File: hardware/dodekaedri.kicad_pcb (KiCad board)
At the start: 4 copper layers, 76.2 x 76.2 mm, 227 parts, among them CON401 BARREL_JACK, J801 HANDSFREE, P301 BNC, P801 TX_SW_WIRE, P802 USB_OTG, P803 UART, P804 PROG, P805 RNG_PINS, P806 CONN_01X08, P807 CONN_01X04, P808 CONN_02X04, P809 BOOT0JMPR, Q501 BCP56, Q502 IRL510, Q801 BSS84, SW801 SW_PUSH, SW802 SW, SW803 SW, SW804 SW, SW806 encoder, SW807 RESET, T301 TRANSFO, T302 TRANSFO, T501 TRANSFO2, T601 TRANSFO2, U201 MIC5365, U202 SI5351A, U401 NCP3170-D, U501 74LVC1G3157, U502 74LVC1G3157, U601 74LVC1G3157, U602 74LVC1G3157, U603 TL972IDR, U701 WM8731, U702 MCP6L02, U801 STM32F401, U802 WM8731

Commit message: intermediate save; closing in on the finished layout
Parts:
- C804, D818, R801, R802, R805, R825, R826, R827, R828, R830, R831, R832, R833, R834, R835, W401: moved to B.Cu
- moved R826 247.2 mm to (106.7, 81.7), turned to 270 degrees
- moved R825 244.0 mm to (106.7, 77.0), turned to 270 degrees
- moved R828 243.8 mm to (106.7, 91.1), turned to 270 degrees
- moved R801 238.2 mm to (121.6, 107.4), turned to 45 degrees
- moved R802 234.9 mm to (124.5, 113.2), turned to 315 degrees
- moved R834 231.9 mm to (114.3, 86.4), turned to 270 degrees
- moved R805 221.1 mm to (122.2, 56.8), turned to 315 degrees
- moved R835 221.1 mm to (114.3, 91.1), turned to 270 degrees
- moved R831 218.3 mm to (114.3, 72.2), turned to 270 degrees
- moved R830 213.2 mm to (113.1, 68.5)
- moved R827 207.0 mm to (106.7, 86.4), turned to 270 degrees
- moved R833 205.7 mm to (114.3, 81.7), turned to 270 degrees
- moved D818 197.4 mm to (117.5, 109.0), turned to 45 degrees
- moved R807 194.4 mm to (118.9, 60.0)
- moved R824 192.6 mm to (114.0, 104.2), turned to 45 degrees
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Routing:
- net Net-(P806-Pad6): track 2.63 -> 71.3 mm
- net Net-(P806-Pad7): track 2.92 -> 65.7 mm
- net /CPU/PB3/SWO: track 4.71 -> 59.5 mm, vias 1 -> 2
- net /CPU/PB2: track 1.29 -> 53.3 mm, vias 1 -> 2
- net /CPU/PB10: track 2.47 -> 44.8 mm, vias 1 -> 2
- net +Vlogic: track 116.1 -> 155.7 mm
- net Net-(C804-Pad1): track 1.04 -> 40.4 mm, vias 1 -> 2
- net Net-(P807-Pad1): track 2.50 -> 40.6 mm
- net Net-(P807-Pad3): track 2.71 -> 40.3 mm
- net Net-(P806-Pad3): track 1.96 -> 39.4 mm
- net Net-(P806-Pad8): track 2.44 -> 34.6 mm
- net Net-(P806-Pad5): track 1.59 -> 26.8 mm
- net Net-(P809-Pad1): track 11.8 -> 33.0 mm
- net GND: track 261.6 -> 281.5 mm, vias 23 -> 26
- net /CPU/VIN_ADC: track 0.00 -> 12.5 mm
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
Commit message: Again, managed to advance layout a bit
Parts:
- C802, Q801, R803, R804: moved to B.Cu
- moved R803 83.9 mm to (132.1, 96.0)
- moved R804 61.5 mm to (139.4, 73.2)
- moved C802 57.6 mm to (135.3, 68.6), turned to 180 degrees
- moved Q801 46.0 mm to (138.4, 70.4), turned to 270 degrees
- moved C805 0.59 mm to (136.8, 77.7)
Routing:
- net /CPU/PC14: track 0.00 -> 73.1 mm, vias 0 -> 2
- net /CPU/PD2: track 4.88 -> 73.1 mm, vias 1 -> 2
- net /CPU/PA3: track 1.11 -> 59.0 mm
- net /CPU/RX_TX: track 11.7 -> 25.2 mm, vias 0 -> 1
- net /CPU/CLK_CPU: track 0.00 -> 12.2 mm, vias 0 -> 1
- net Net-(P806-Pad5): track 26.8 -> 35.2 mm
- net +Vlogic: track 155.7 -> 162.3 mm
- net GND: track 281.5 -> 285.1 mm, vias 26 -> 28
- net Net-(Q801-Pad2): track 0.00 -> 2.18 mm
- net /CPU/UI_SW_GRID1: track 12.8 -> 12.3 mm

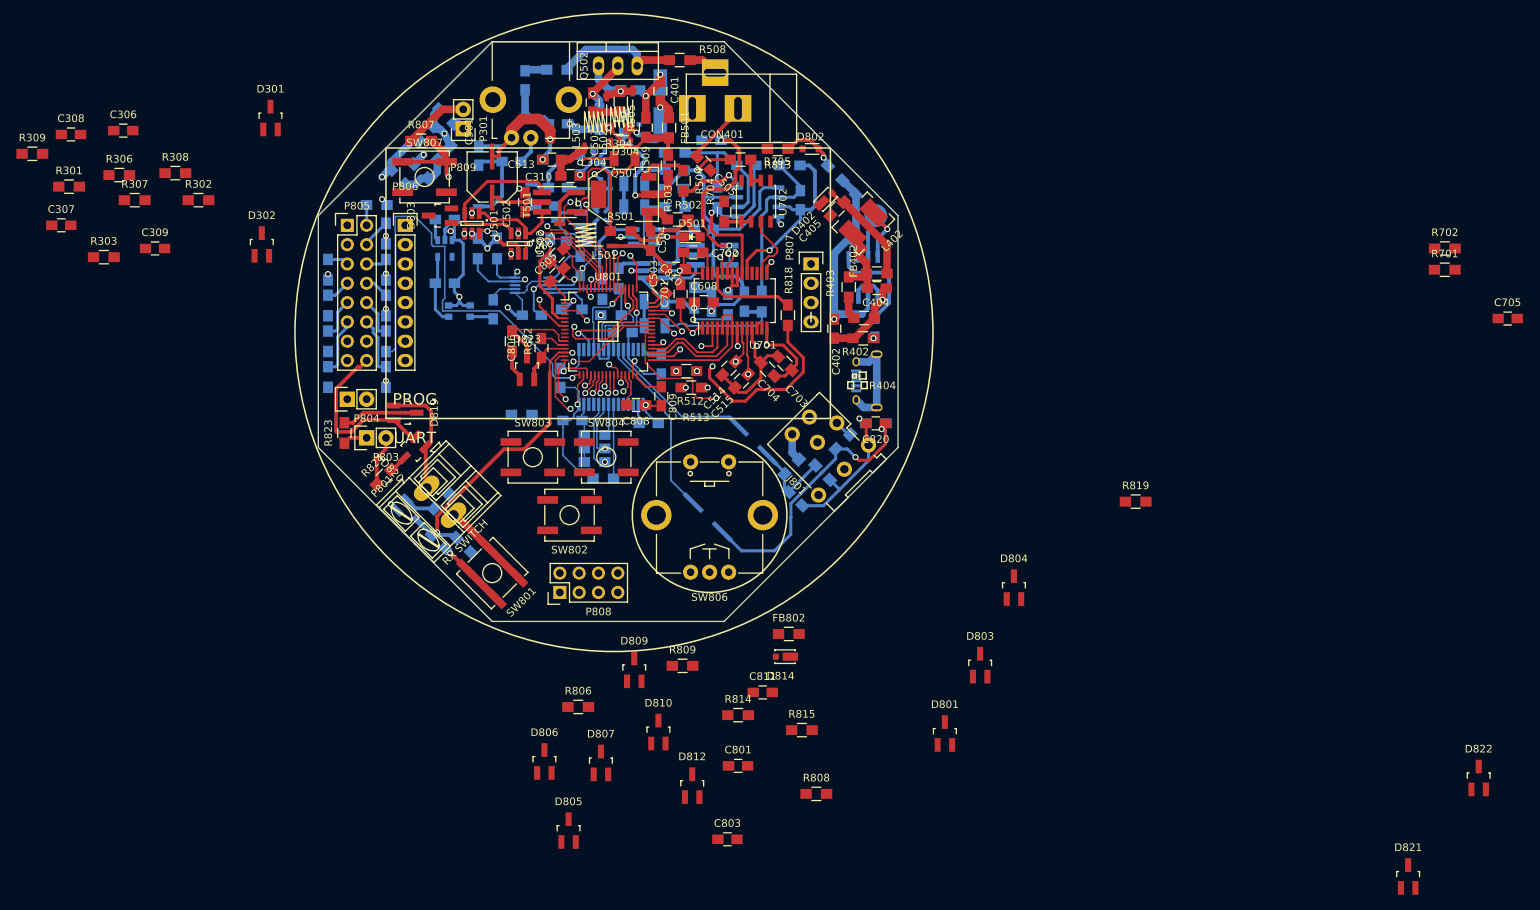
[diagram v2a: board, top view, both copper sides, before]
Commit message: Quite a few routing bugs fixed and backup-commiting
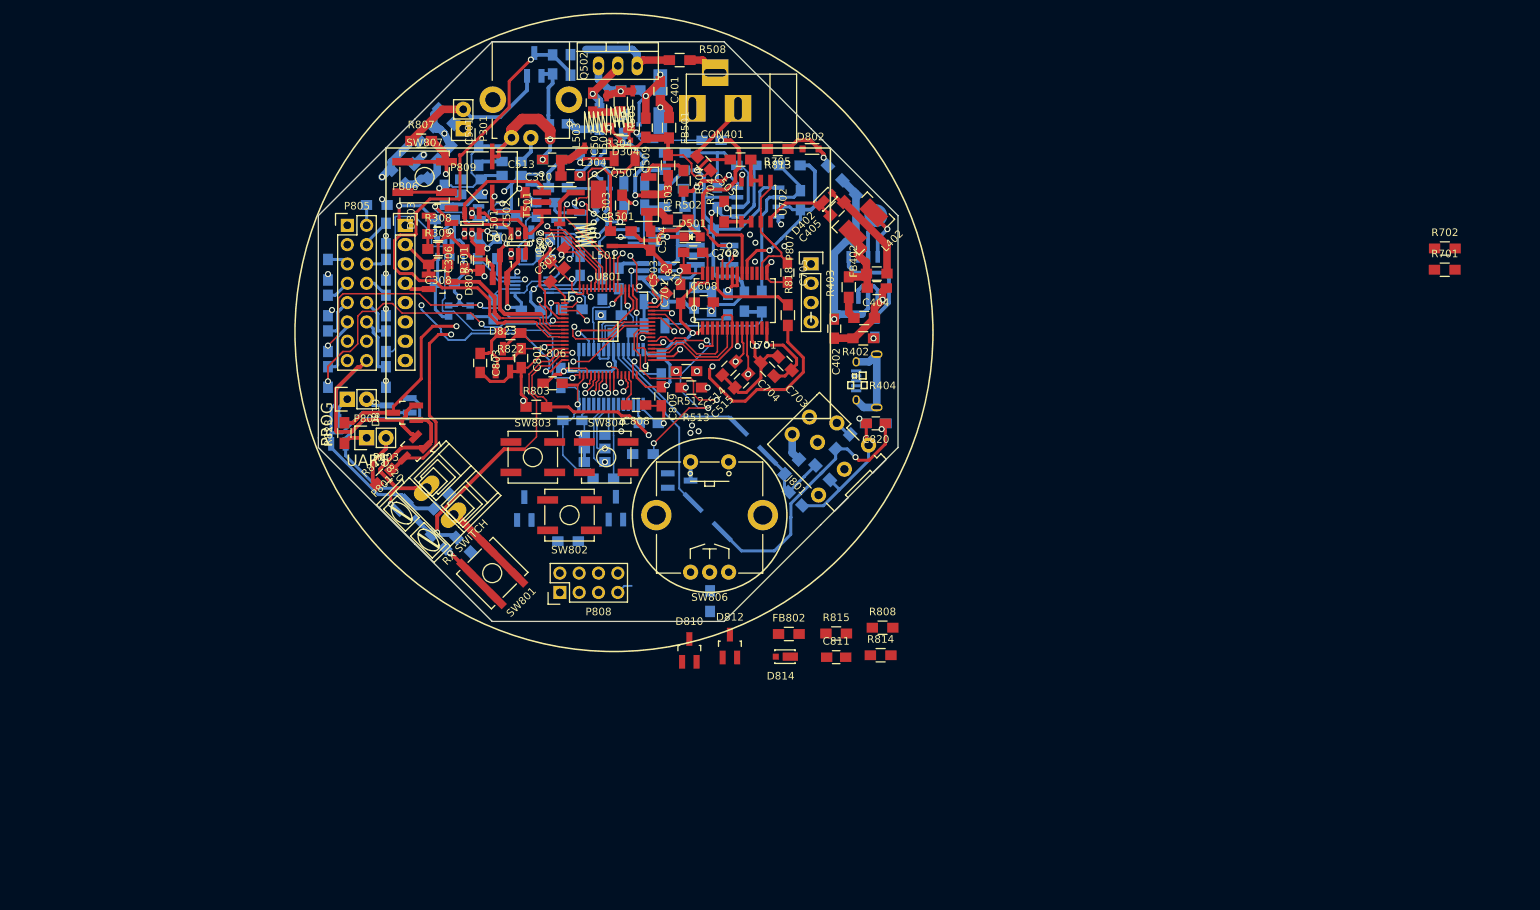
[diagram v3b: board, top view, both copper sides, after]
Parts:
- removed D805: 1N914, dodekaedri:SOT-23_HS_2-1-3
- C307, C309, D301, D302, D801, D806, D807, D809, D821, D822, R302, R306, R307, R806, R809, R819: moved to B.Cu
- R803: moved to F.Cu
- moved D822 156.6 mm to (108.1, 98.3), turned to 180 degrees
- moved D821 146.5 mm to (115.9, 94.8), turned to 270 degrees
- moved D801 103.2 mm to (133.8, 50.0), turned to 180 degrees
- moved C705 94.9 mm to (167.1, 77.3), turned to 270 degrees
- moved D803 87.1 mm to (121.4, 78.5), turned to 270 degrees
- moved D804 79.6 mm to (129.3, 76.6)
- moved C803 70.5 mm to (126.7, 89.2), turned to 270 degrees
- moved R303 68.5 mm to (145.4, 68.5), turned to 90 degrees
- moved R819 65.1 mm to (148.1, 101.2), turned to 180 degrees
- moved C801 60.7 mm to (132.1, 88.6), turned to 270 degrees
- moved R301 54.9 mm to (126.7, 75.7), turned to 90 degrees
- moved R309 54.8 mm to (121.2, 74.2)
- moved C308 51.2 mm to (121.2, 76.3), turned to 180 degrees
- moved C307 50.5 mm to (122.0, 67.1), turned to 90 degrees
- moved C306 48.0 mm to (124.7, 75.6), turned to 90 degrees
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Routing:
- net +Vlogic: track 162.3 -> 287.8 mm, vias 11 -> 18
- net GND: track 285.1 -> 399.4 mm, vias 28 -> 31
- net Net-(R803-Pad2): track 8.89 -> 93.9 mm, vias 1 -> 3
- net /CPU/PA_CURR_ADC: track 2.90 -> 73.7 mm, vias 0 -> 1
- net /CPU/SWDIO: track 2.83 -> 72.7 mm
- net /CPU/UI_SW_GRID3: track 12.2 -> 82.0 mm, vias 1 -> 3
- net /CPU/PC13: track 0.00 -> 63.1 mm, vias 0 -> 2
- net /CPU/SWCLK: track 4.53 -> 66.3 mm, vias 1 -> 2
- net /CPU/UI_SW_GRID1: track 12.3 -> 72.6 mm, vias 1 -> 3
- net /CPU/UI_SW_GRID2: track 14.0 -> 73.2 mm, vias 1 -> 3
- net Net-(C306-Pad1): track 1.26 -> 48.1 mm, vias 1 -> 5
- net /CPU/PC15: track 0.00 -> 42.0 mm, vias 0 -> 3
- net /CPU/PH1: track 0.00 -> 41.1 mm, vias 0 -> 3
- net /CPU/UART_TX: track 14.6 -> 55.7 mm, vias 1 -> 2
- net Net-(D303-Pad2): track 0.00 -> 39.3 mm, vias 0 -> 4
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
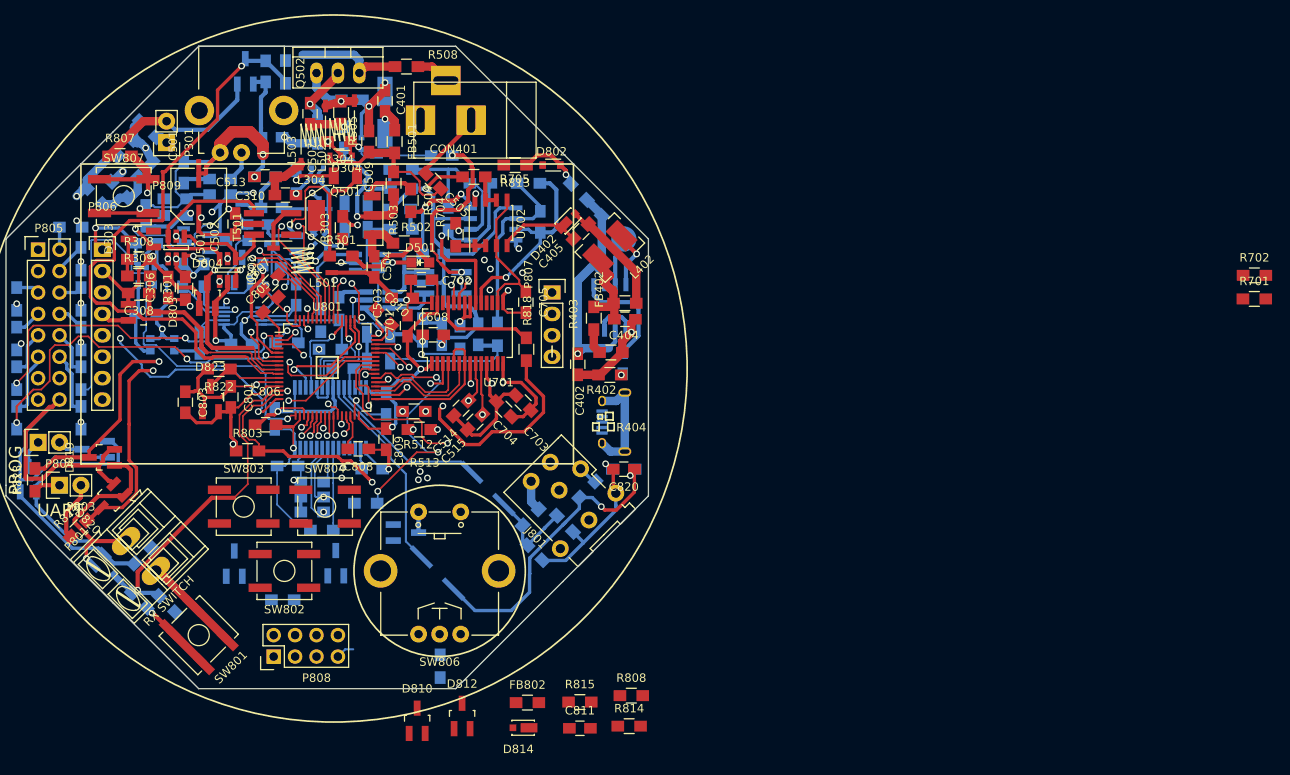
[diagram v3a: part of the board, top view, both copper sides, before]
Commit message: All components are placed. GND and +Vlogic copper fills still undone
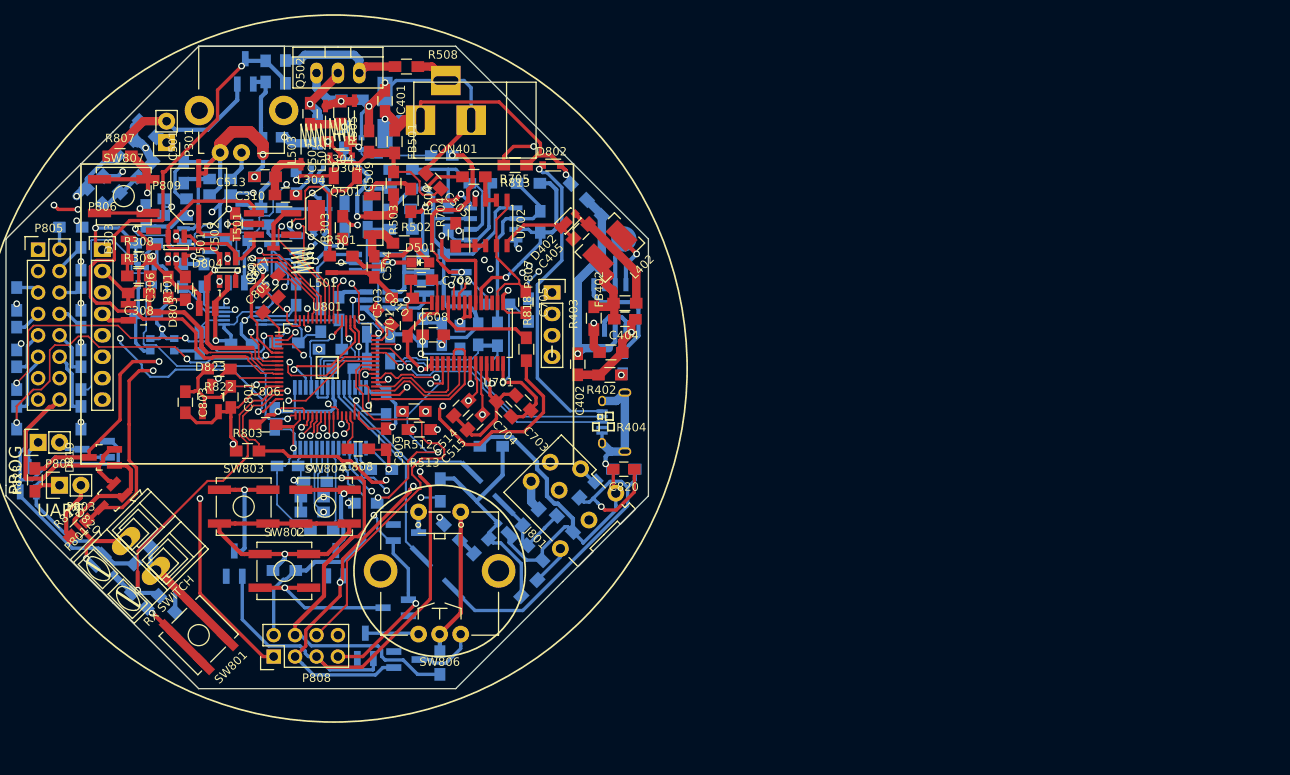
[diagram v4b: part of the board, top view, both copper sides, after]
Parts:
- added D805: 1N914, dodekaedri:SOT-23_HS_2-1-3, B.Cu at (151.6, 113.6)
- C811, D810, D812, D814, FB802, R701, R702, R808, R814, R815: moved to B.Cu
- moved R702 89.8 mm to (163.7, 77.6), turned to 180 degrees
- moved R701 86.1 mm to (167.4, 78.3), turned to 90 degrees
- moved R808 33.9 mm to (163.0, 94.4), turned to 180 degrees
- moved R814 31.2 mm to (158.3, 104.6), turned to 315 degrees
- moved R815 30.1 mm to (156.9, 99.6), turned to 90 degrees
- moved C811 24.6 mm to (161.8, 106.3), turned to 45 degrees
- moved D814 23.9 mm to (164.2, 104.0), turned to 315 degrees
- moved FB802 13.6 mm to (167.5, 111.3), turned to 45 degrees
- moved D810 10.8 mm to (148.0, 118.1), turned to 180 degrees
- moved D812 9.40 mm to (152.9, 119.7), turned to 90 degrees
- moved R806 3.49 mm to (138.4, 109.2), turned to 180 degrees
- moved R507 1.13 mm to (118.0, 63.3)
- moved C818 1.08 mm to (149.9, 97.2)
- moved D302 0.67 mm to (132.7, 73.6)
- moved R809 0.38 mm to (156.9, 120.1)
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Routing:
- net /CPU/UI_SW_GRID4: track 12.2 -> 139.7 mm, vias 1 -> 3
- net /CPU/VIN_ADC: track 9.43 -> 117.9 mm, vias 0 -> 4
- net /CPU/UI_SW_GRID2: track 73.2 -> 130.8 mm
- net Net-(P808-Pad4): track 17.4 -> 61.9 mm
- net GND: track 399.4 -> 440.7 mm
- net /CPU/UI_SW_GRID3: track 82.0 -> 122.4 mm, vias 3 -> 4
- net Net-(D802-Pad2): track 0.00 -> 37.8 mm, vias 0 -> 1
- net Net-(R806-Pad2): track 0.00 -> 37.5 mm, vias 0 -> 1
- net Net-(D302-Pad1): track 0.00 -> 33.2 mm, vias 0 -> 2
- net /CPU/UI_SW_GRID1: track 72.6 -> 103.6 mm, vias 3 -> 4
- net Net-(P808-Pad6): track 20.2 -> 50.7 mm, vias 1 -> 0
- net Vin_net: track 11.3 -> 41.4 mm
- net Net-(C811-Pad2): track 0.00 -> 28.6 mm
- net Net-(P808-Pad2): track 13.6 -> 42.1 mm
- net /CPU/PA11/USB: track 3.70 -> 31.0 mm
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
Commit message: layout done,d
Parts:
- moved C608 2.36 mm to (153.9, 80.3), turned to 90 degrees
- moved R303 1.75 mm to (145.5, 70.3), turned to 0 degrees
- moved C810 1.17 mm to (149.5, 78.2)
- moved C701 0.65 mm to (152.4, 80.0)
- moved Q501 0.61 mm to (146.1, 66.8)
- moved D501 0.46 mm to (154.2, 72.4)
- moved C503 0.46 mm to (152.0, 76.6)
- moved R503 0.20 mm to (151.6, 63.2)
- moved R501 0.06 mm to (145.1, 71.9)
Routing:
- net +Vlogic: track 300.4 -> 407.5 mm, vias 16 -> 39
- net GND: track 440.7 -> 519.3 mm, vias 31 -> 43
- net Vin_net: track 41.4 -> 19.8 mm
- net /CPU/VIN_ADC: track 117.9 -> 113.6 mm
- net /CPU/RX_TX: track 26.8 -> 31.0 mm
- net /CPU/SWCLK: track 68.1 -> 71.6 mm
- net /RX_chain/RX_BIAS: track 56.4 -> 59.8 mm
- net Net-(R513-Pad1): track 31.5 -> 34.5 mm
- net Net-(D303-Pad2): track 39.3 -> 42.0 mm
- net Net-(L501-Pad1): track 5.49 -> 7.78 mm
- net /CPU/UI_SW_GRID1: track 103.6 -> 105.5 mm
- net /CPU/PB10: track 45.3 -> 46.8 mm
- net Net-(R818-Pad1): track 33.3 -> 34.8 mm
- net Net-(C306-Pad1): track 49.4 -> 48.0 mm
- net /CPU/UI_SW_GRID4: track 139.7 -> 141.0 mm
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- added copper zone on In1.Cu, net +Vlogic
- added copper zone on In2.Cu, net +Vlogic
- added copper zone on B.Cu, net GND
- added copper zone on F.Cu, net GND
- added copper zone on In1.Cu, net GND
- added copper zone on In2.Cu, net GND
- added copper zone on F.Cu, net Vin_net
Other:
- board text added: "2017"
- board text added: "exla - oh2ehk tejeez - oh2eat Dodekaedri v1.0"
- board text added: "oh2ti polyteknikkojen radiokerho r.y."

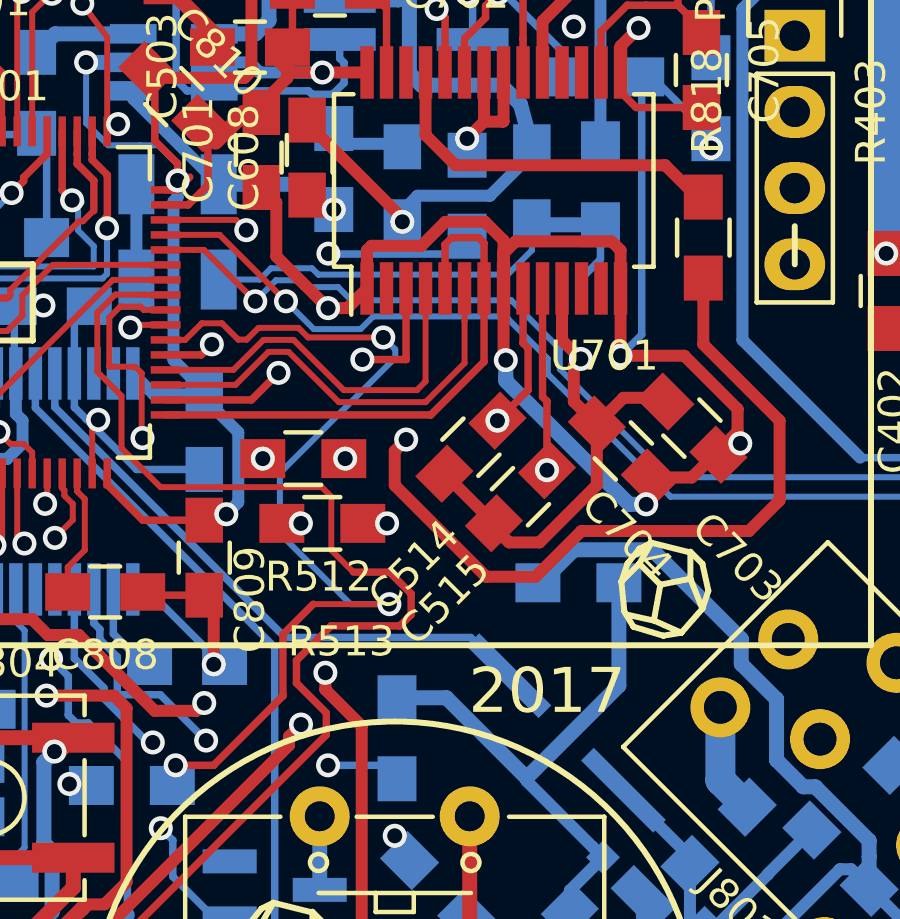
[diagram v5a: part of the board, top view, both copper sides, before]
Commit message: fixed serious schematic and thus layout bug
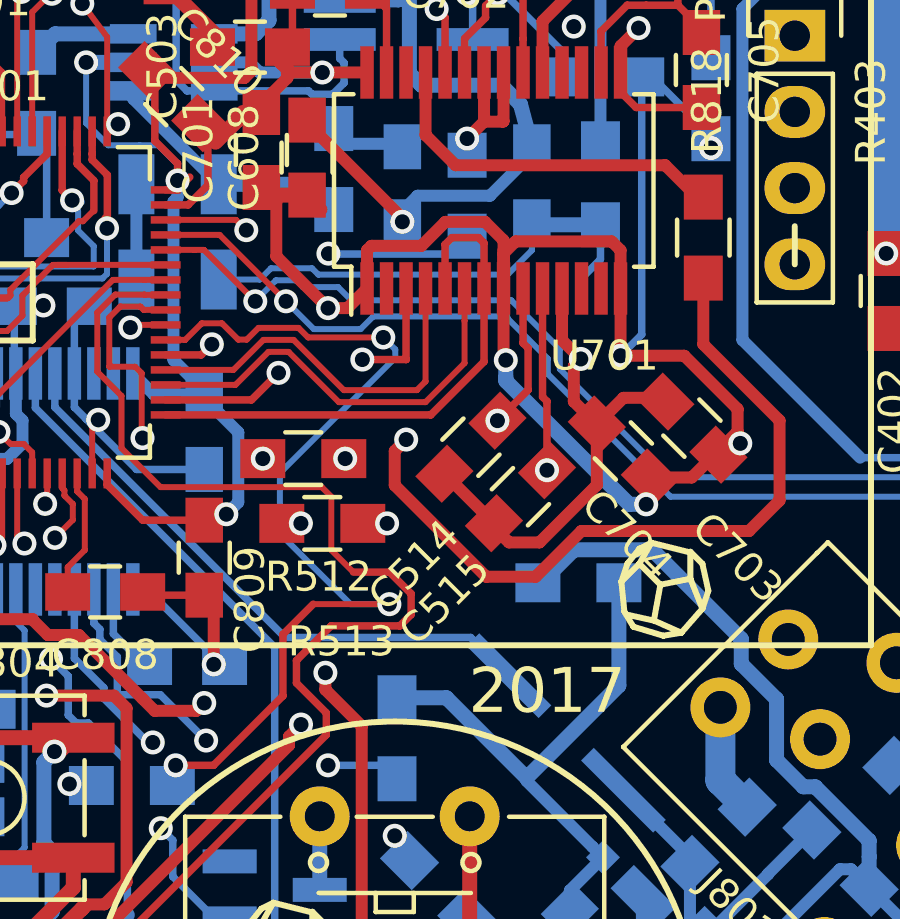
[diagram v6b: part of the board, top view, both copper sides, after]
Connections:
- C608 pad 1: Net-(C608-Pad1) -> +Vlogic
- L602 pad 1: Net-(C608-Pad1) -> Net-(L602-Pad1)
- R602 pad 1: Net-(C608-Pad1) -> Net-(L602-Pad1)
- U602 pad 4: Net-(C608-Pad1) -> Net-(L602-Pad1)
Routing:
- net Net-(C608-Pad1): track 9.81 -> 0.00 mm, vias 1 -> 0
- net Net-(L602-Pad1): track 0.00 -> 8.69 mm
- net +Vlogic: track 407.5 -> 409.8 mm
